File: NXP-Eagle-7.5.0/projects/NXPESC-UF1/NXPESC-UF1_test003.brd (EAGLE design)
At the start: 50.8 x 25.4 mm, 59 parts, among them J2 FLH1-03SZ-S3A-T, U1 MKV31F512VLL12-M, U10 PSMN1R4-30YLD, U11 PSMN1R4-30YLD, U12 PSMN1R4-30YLD, U13 PSMN1R4-30YLD, U8 PSMN1R4-30YLD, U9 PSMN1R4-30YLD

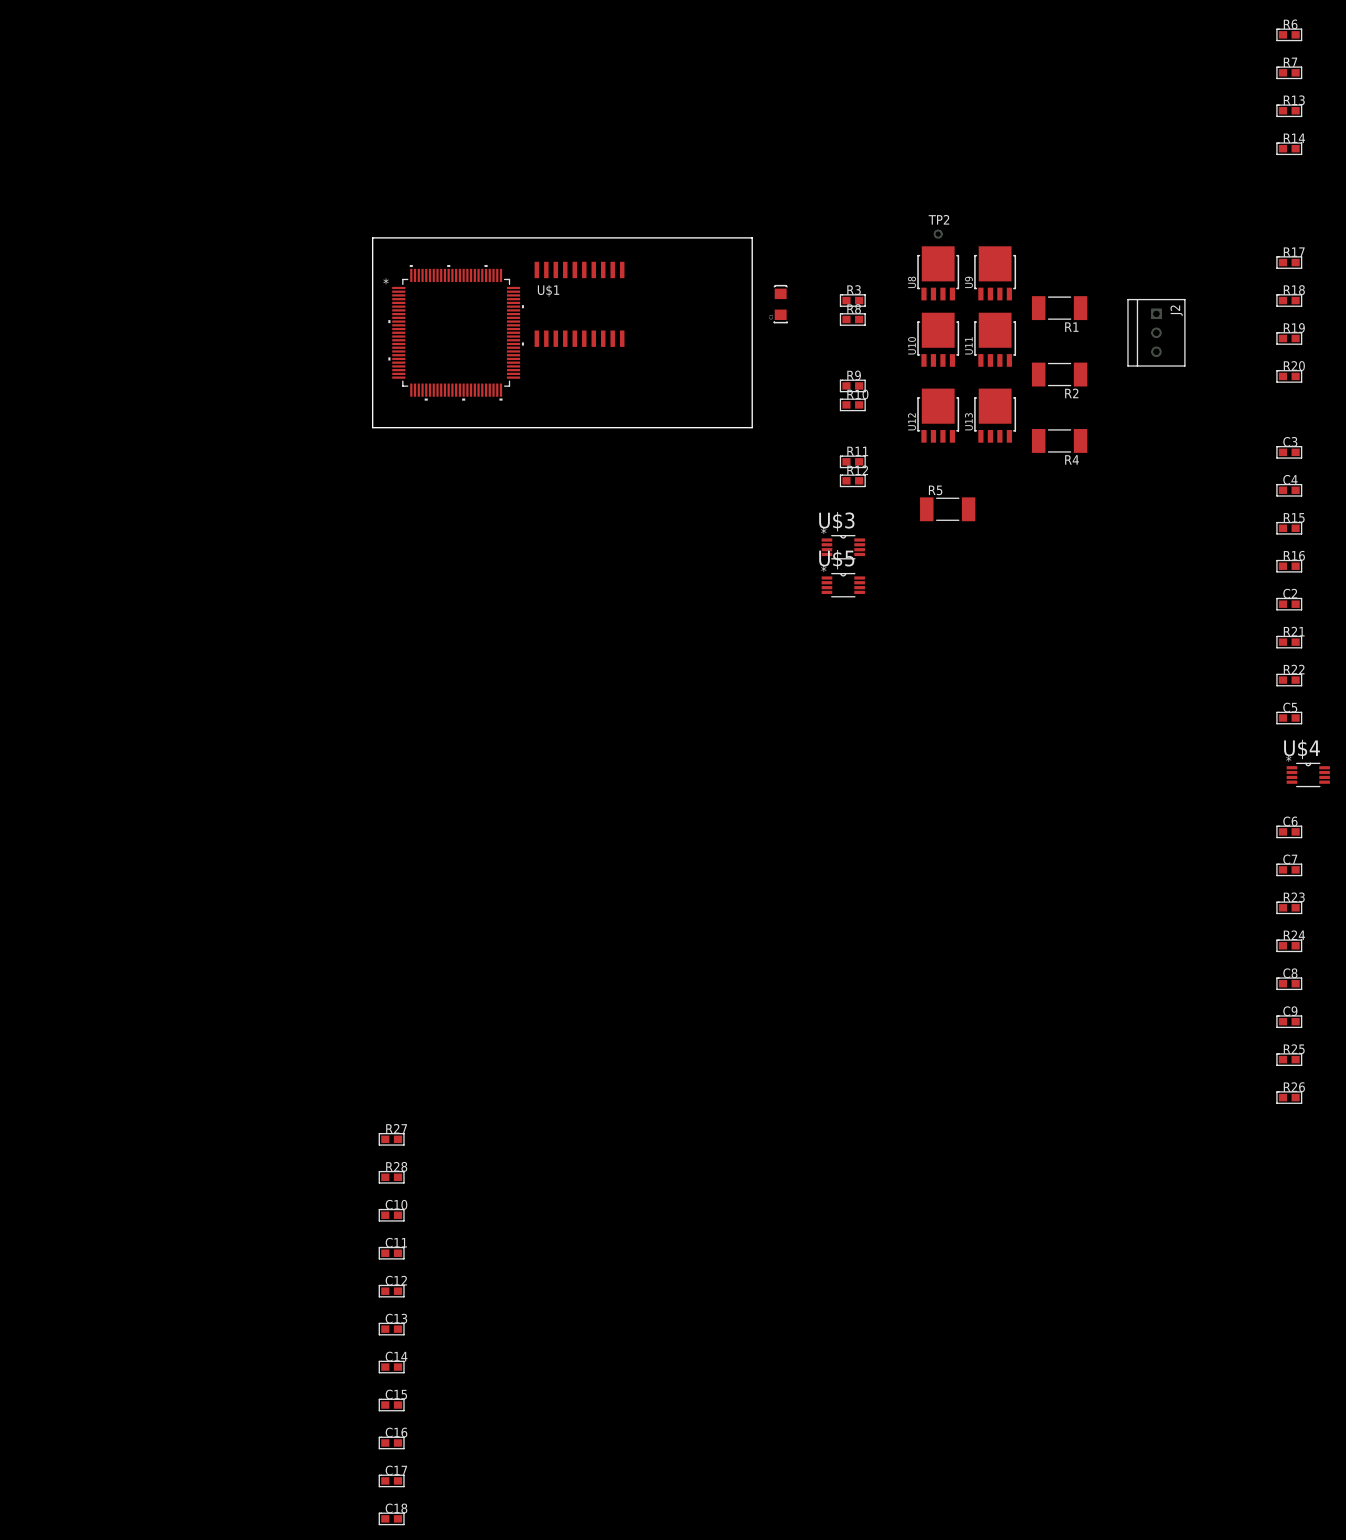
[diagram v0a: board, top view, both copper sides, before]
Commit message: Trial placement on board, Note that the schematic is not complete yet. Also created the 64 pin KV 31 Part.
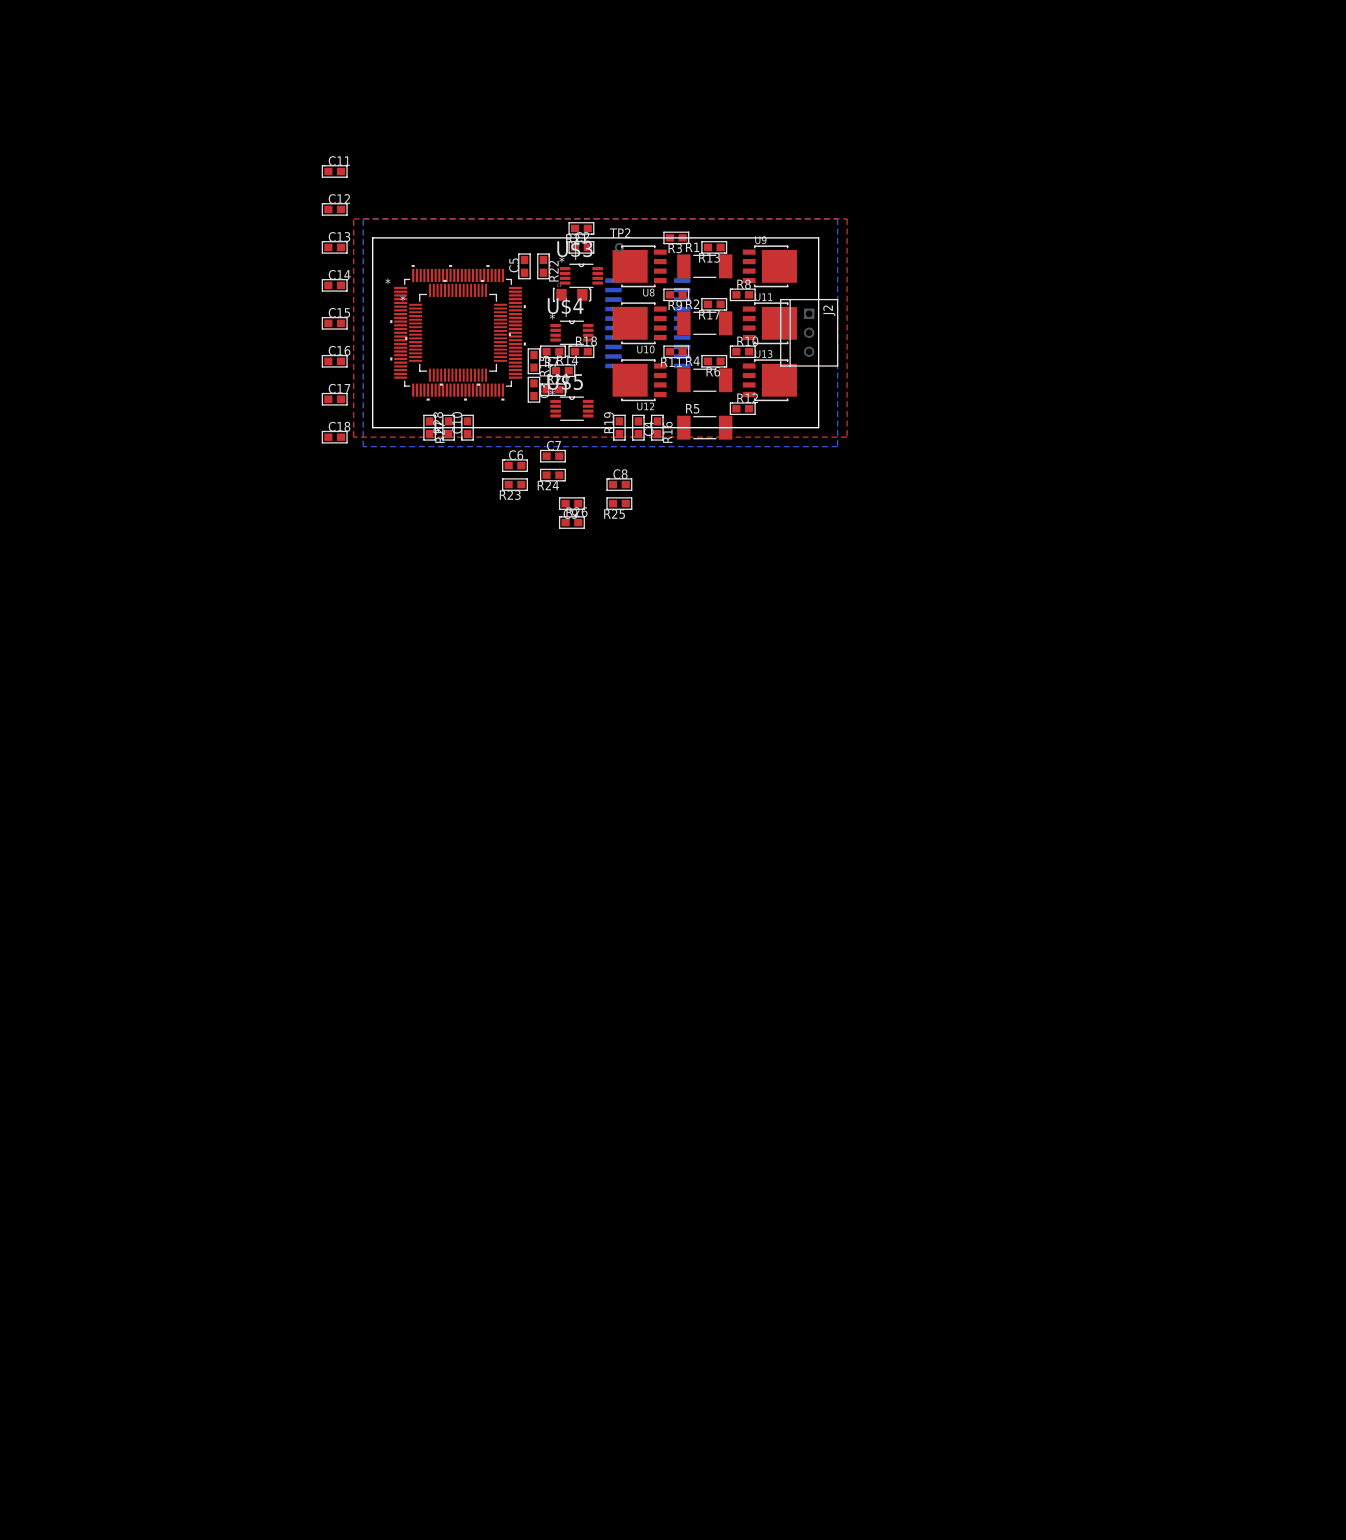
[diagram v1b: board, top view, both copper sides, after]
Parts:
- added U2: MKV31F512VLH12-M, MKV31F512VLH12:LQFP-64_10X10X1_6-M
- moved C11 145.0 mm to (-5.08, 34.3)
- moved C12 145.0 mm to (-5.08, 29.2)
- moved C13 145.0 mm to (-5.08, 24.1)
- moved C14 145.0 mm to (-5.08, 19.1)
- moved C15 145.0 mm to (-5.08, 14.0)
- moved C17 145.0 mm to (-5.08, 3.81)
- moved C18 145.0 mm to (-5.08, -1.27)
- moved C16 145.0 mm to (-5.08, 8.89)
- moved R26 123.1 mm to (26.7, -12.7)
- moved C5 118.9 mm to (20.3, 21.6), turned to 90 degrees
- moved C9 118.4 mm to (26.7, -10.2), turned to 180 degrees
- moved R23 118.1 mm to (19.1, -7.62), turned to 180 degrees
- moved R24 117.0 mm to (24.1, -6.35), turned to 180 degrees
- moved R25 116.5 mm to (33.0, -10.2), turned to 180 degrees
- moved U$4 115.0 mm to (26.7, 12.7)
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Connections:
- new net VDD_2: U2.30
- new net VDD_3: U1.40, U2.48
- new net VDD_7: U1.89
- new net VSS_2: U2.31
- new net VSS_3: U1.41
- new net VSS_7: U1.88
- net +3V3: now also U2.20, U2.3, U2.47; no longer U1.40, U1.89
- net GND: now also U2.21, U2.32, U2.4; no longer U1.41, U1.88
- net N$5: now also U2.44
- net N$6: now also U2.45
- net N$7: now also U2.50; no longer U1.77
- net N$8: now also U2.49; no longer U1.76
- net VDDA: now also U2.13
- net VREFH: now also U2.14
- net VREFL: now also U2.15
- net VSSA: now also U2.16
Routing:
- added copper zone on layer 1, net GND
- added copper zone on layer 16, net GND
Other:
- board size 50.8 x 25.4 mm -> 59.7 x 25.4 mm

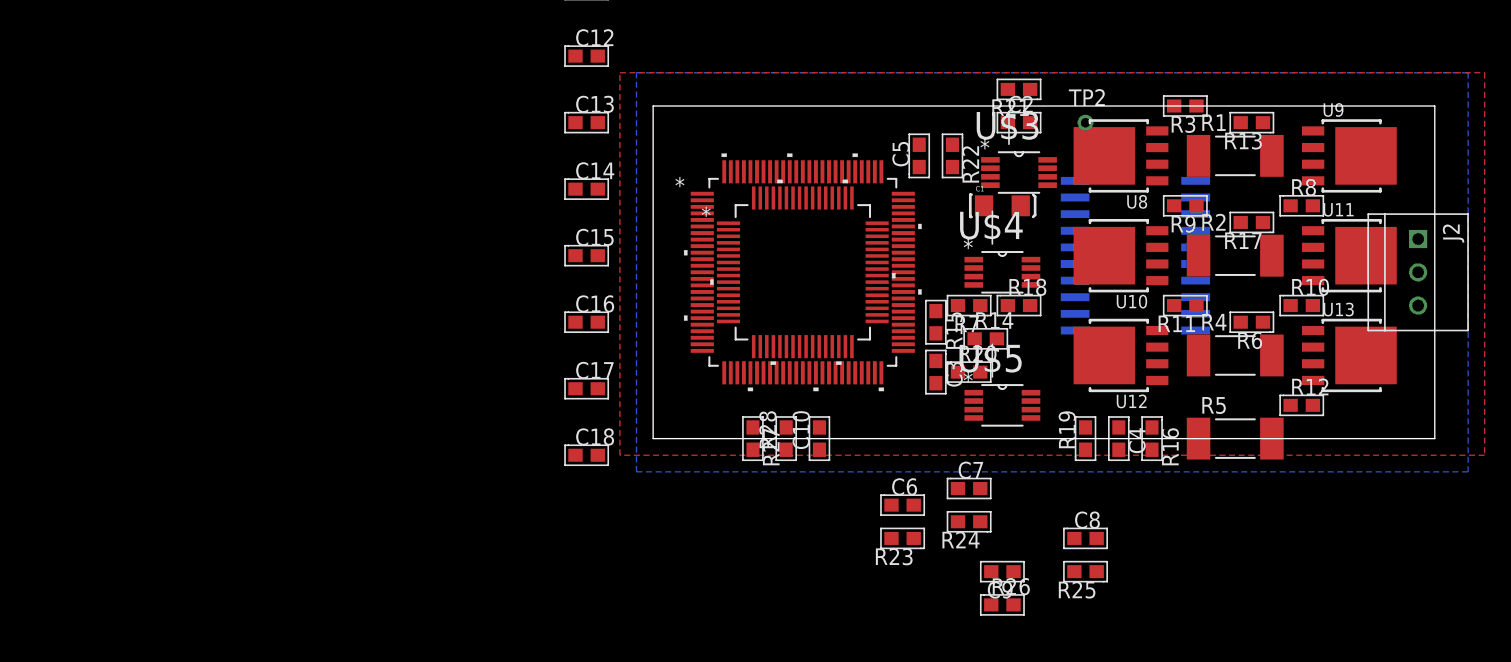
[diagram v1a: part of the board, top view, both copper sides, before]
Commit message: Working on Layout trying to arrange drivers fets and opamps
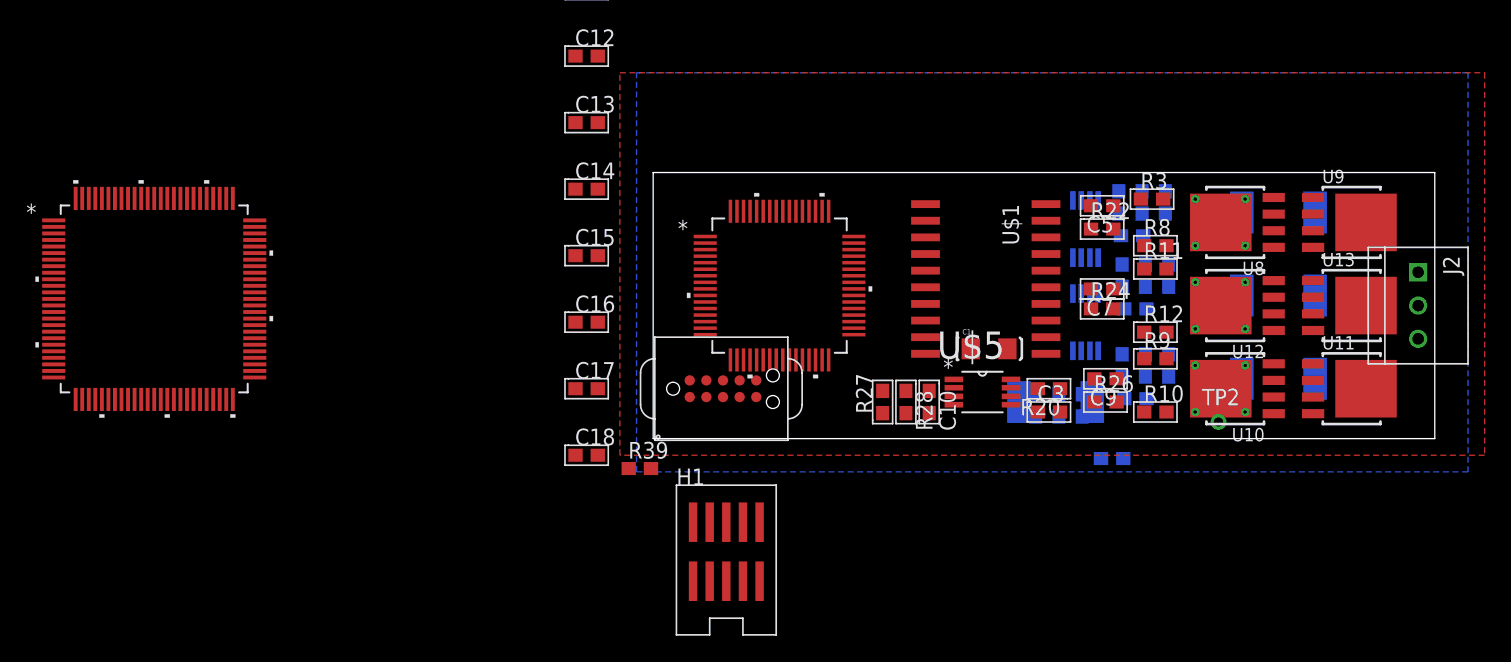
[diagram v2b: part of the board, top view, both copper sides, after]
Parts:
- added H1: DNI(HDR-TSHSM-5-05-D-02-G-V-XXX-TB-0-LF), etc-connector-002a:HD2X5-SMD-0.05"
- added H3: TC2050-IDCNH, etc-connector-003a:TC2050-IDC-NOHOLES
- added R39: RESC0603-4K7-5, etc_rcl:C0603
- moved U1 49.6 mm to (-38.1, 10.7)
- moved R23 27.3 mm to (37.6, 12.4), flipped to the bottom, turned to 90 degrees
- moved TP2 25.0 mm to (43.2, 1.27)
- moved C6 24.3 mm to (35.8, 12.4), flipped to the bottom, turned to 270 degrees
- moved R24 19.2 mm to (34.3, 9.91), turned to 0 degrees
- moved C7 18.3 mm to (34.3, 11.4), turned to 180 degrees
- moved R26 17.4 mm to (34.5, 2.79)
- moved R15 17.0 mm to (35.1, -1.52), flipped to the bottom, turned to 180 degrees
- moved C9 16.7 mm to (34.5, 4.57)
- moved R25 16.0 mm to (35.8, 5.59), flipped to the bottom, turned to 90 degrees
- moved C5 14.5 mm to (34.3, 17.8), turned to 180 degrees
- moved R5 14.0 mm to (30.7, 2.79), flipped to the bottom, turned to 180 degrees
- moved C8 14.0 mm to (37.6, 5.59), flipped to the bottom, turned to 270 degrees
- moved R10 13.8 mm to (38.4, 2.03)
- moved R14 13.7 mm to (36.6, 15.5), flipped to the bottom
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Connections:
- net N$15 renamed CS_DCB_H
- net N$16 renamed CS_DCB_L
- removed net CA_A_L: R14.2
- removed net VDD: C1.A, U$1.12
- new net N$15: H1.7, H3.4
- new net N$16: H1.8, H3.7
- new net N$18: H1.9, H3.5
- new net RESET_B: H1.10, H3.6, U2.34
- new net SWD_CLK: H1.4, H3.9, U2.22
- new net SWD_DIO: H1.2, H3.10, R39.1, U2.25
- new net TRACE_SWO: H1.6, H3.8, U2.24
- net +3V3: now also C1.A, H1.1, H3.1, R39.2, U$1.12
- net CS_A_L: now also R14.2
- net GND: now also H1.3, H1.5, H3.2, H3.3
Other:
- board size 59.7 x 25.4 mm -> 59.7 x 20.3 mm

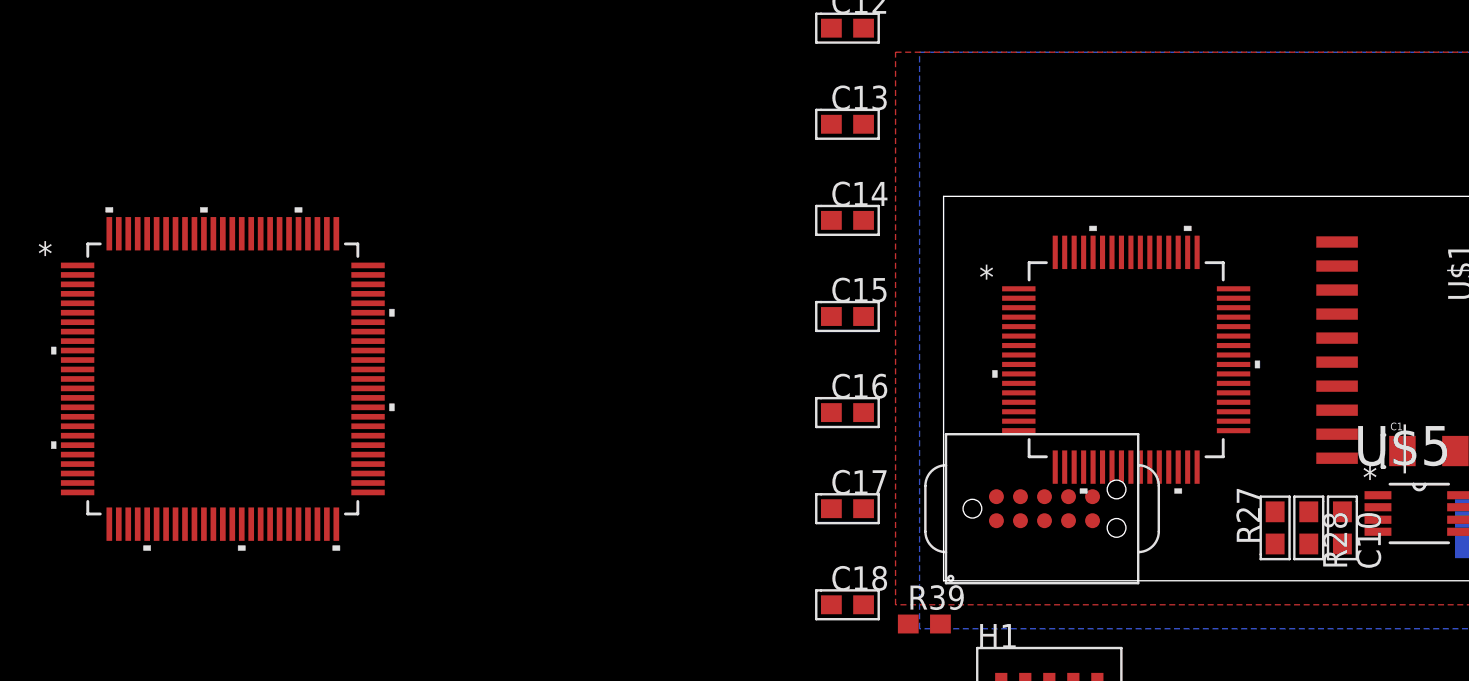
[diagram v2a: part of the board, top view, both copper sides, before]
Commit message: Add PHY and DF13 4-pin CAN conn to SCH
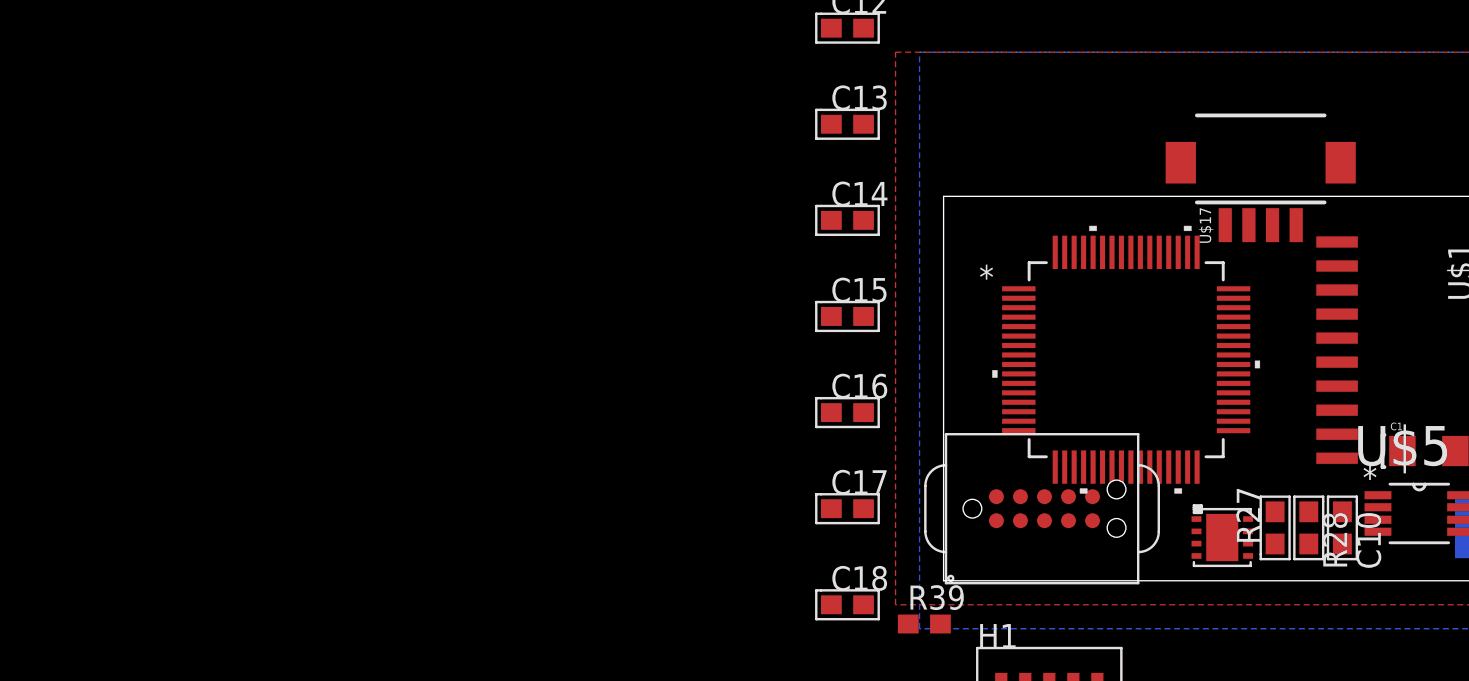
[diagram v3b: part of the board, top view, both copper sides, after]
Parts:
- removed U1: MKV31F512VLL12-M, MKV31F512VLL12:LQFP-100_14X14X1_7-M
- added U$15: TJA1042TK/3, TJA1042T:HVSON8
- added U$17: DF13-4P-1.25H, pixhawk2:DF13A-4P-1.25H
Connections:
- removed net VDD_7: U1.89
- removed net VSS_3: U1.41
- removed net VSS_7: U1.88
- new net CAN0_RX: U$15.4, U2.29
- new net CAN0_TX: U$15.1, U2.28
- new net N$22: U$15.7, U$17.2
- new net N$23: U$15.6, U$17.3
- new net STB: U$15.8, U2.27
- new net VCC: U$15.3
- net +3V3: now also U$15.5; no longer U1.30, U1.48, U1.61, U1.75, U1.8
- net GND: now also U$15.2, U$17.4; no longer U1.29, U1.49, U1.60, U1.74, U1.9
- net N$5: no longer U1.71
- net N$6: no longer U1.72
- net VDDA: no longer U1.22
- net VDD_3: no longer U1.40
- net VREFH: no longer U1.23
- net VREFL: no longer U1.24
- net VSSA: no longer U1.25
